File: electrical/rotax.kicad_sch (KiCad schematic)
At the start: 22 parts

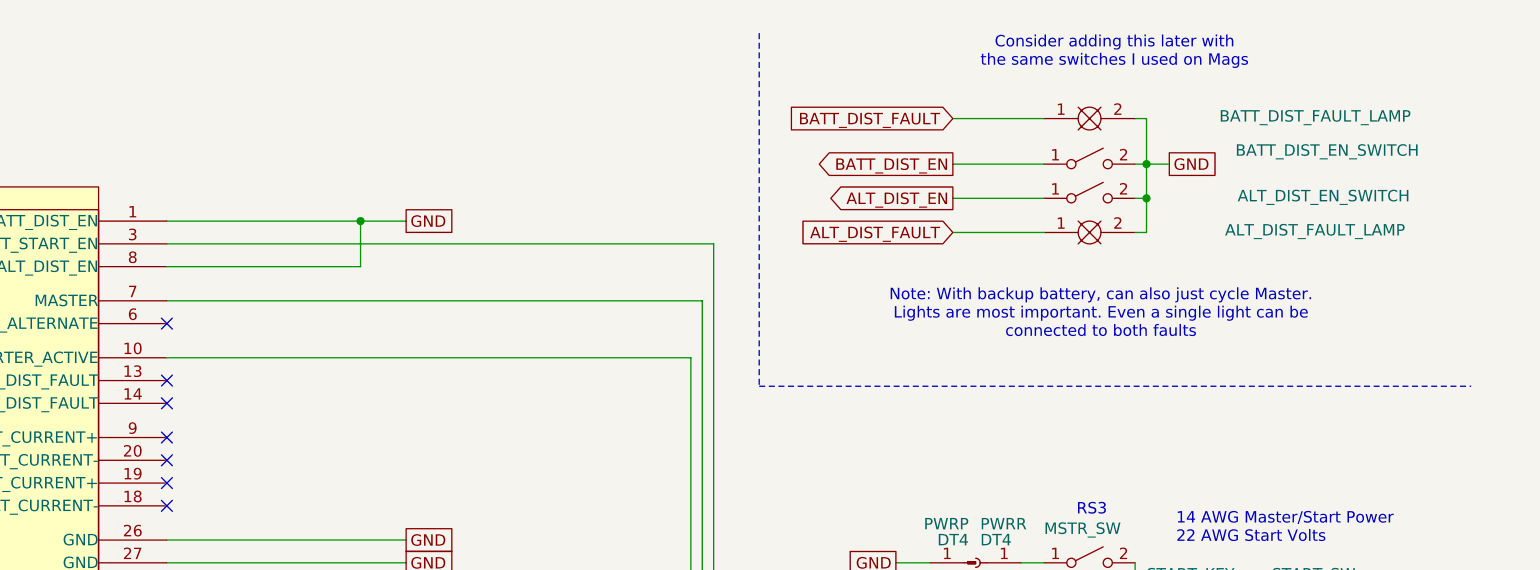
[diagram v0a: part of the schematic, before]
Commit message: Added PPS Indicator circuit
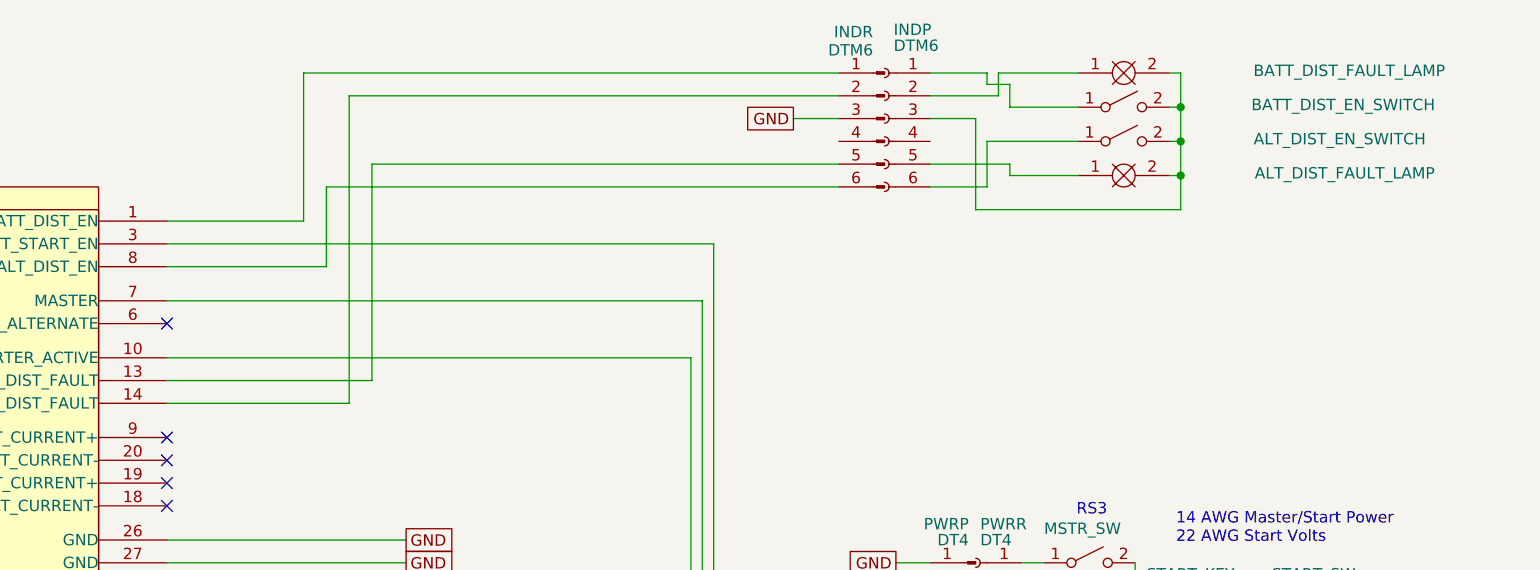
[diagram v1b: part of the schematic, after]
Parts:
- added INDP: DTM6, symbol Connector:Conn_01x06_Socket
- added INDR: DTM6, symbol Connector:Conn_01x06_Pin
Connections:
- net Earth: now also INDR.3 (Pin_3); no longer ALT_DIST_EN_SWITCH.2 (B), ALT_DIST_FAULT_LAMP.2, BATT_DIST_EN_SWITCH.2 (B), BATT_DIST_FAULT_LAMP.2, PPS.1 (BATT_DIST_EN), PPS.8 (ALT_DIST_EN)
- net at PPS.13 (ALT_DIST_FAULT): now also INDR.5 (Pin_5)
- net at PPS.14 (BATT_DIST_FAULT): now also INDR.2 (Pin_2)
- net ALT_DIST_EN: no longer names the net of ALT_DIST_EN_SWITCH.1 (A)
- net ALT_DIST_EN: now also INDP.6 (Pin_6)
- net ALT_DIST_FAULT: no longer names the net of ALT_DIST_FAULT_LAMP.1
- net ALT_DIST_FAULT: now also INDP.5 (Pin_5)
- net BATT_DIST_EN: no longer names the net of BATT_DIST_EN_SWITCH.1 (A)
- net BATT_DIST_EN: now also INDP.1 (Pin_1)
- net BATT_DIST_FAULT: no longer names the net of BATT_DIST_FAULT_LAMP.1
- net BATT_DIST_FAULT: now also INDP.2 (Pin_2)
- new net: ALT_DIST_EN_SWITCH.2 (B), ALT_DIST_FAULT_LAMP.2, BATT_DIST_EN_SWITCH.2 (B), BATT_DIST_FAULT_LAMP.2, INDP.3 (Pin_3)
- new net: INDR.1 (Pin_1), PPS.1 (BATT_DIST_EN)
- new net: INDR.6 (Pin_6), PPS.8 (ALT_DIST_EN)
- no-connect marks 10 -> 8
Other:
- note removed: "Consider adding this later with the same switches I used on Mags"
- note removed: "Note: With backup battery, can also just cycle Master. Lights are most important. Even a single light can be connected to both faults"
- moved on the sheet: ALT_DIST_EN_SWITCH, ALT_DIST_FAULT_LAMP, BATT_DIST_EN_SWITCH, BATT_DIST_FAULT_LAMP

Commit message: Corrected all rececptacle/plug polarity and naming.
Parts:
- IND: renamed from INDR; value DTM6 -> DTM6R
- IND: renamed from INDP; value DTM6 -> DTM6P
- MSTR: renamed from PWRR; value DT4 -> DT4P
- MSTR: renamed from PWRP; value DT4 -> DT4R
- PLD: renamed from IGNP; value DT6 -> DT6R
- PLD: renamed from IGNP; value DT6 -> DT6P
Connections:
- net Earth: now also MSTR.1 (Pin_1), PLD.2 (Pin_2), PLD.4 (Pin_4); no longer MSTR.1 (Pin_1), PLD.2 (Pin_2), PLD.4 (Pin_4)
- net IGN_PWR: now also PLD.3 (Pin_3); no longer PLD.3 (Pin_3)
- net START_VOLTS: now also MSTR.4 (Pin_4); no longer MSTR.4 (Pin_4)
- net at MSTR_SW.1 (A): now also MSTR.1 (Pin_1); no longer MSTR.1 (Pin_1)
- net at MSTR.2 (Pin_2): now also PPS.7 (MASTER); no longer MSTR_SW.2 (B)
- net at MSTR.3 (Pin_3): now also PPS.3 (MAIN_BATT_START_EN); no longer START_KEY.1 (A)
- net at PLD.1 (Pin_1): now also PLEADL_SW.2 (B); no longer SFLY_LEFT. (PLEAD)
- net at SFLY_RIGHT. (PLEAD): now also PLD.6 (Pin_6); no longer PLD.3 (Pin_3)
- net at PLD.6 (Pin_6): now also PLEADR_SW.2 (B); no longer SFLY_RIGHT. (PLEAD)
- net at PLD.1 (Pin_1): now also SFLY_LEFT. (PLEAD); no longer PLEADL_SW.2 (B)
- net at PLD.5 (Pin_5): now also PLD.4 (Pin_4), SFLY_RIGHT. (PLEAD)
- net at PPS.10 (STARTER_ACTIVE): now also MSTR.4 (Pin_4); no longer MSTR.4 (Pin_4)
- net at MSTR.3 (Pin_3): now also START_KEY.1 (A); no longer PPS.3 (MAIN_BATT_START_EN)
- net at MSTR.2 (Pin_2): now also MSTR_SW.2 (B); no longer PPS.7 (MASTER)
- new net: PLD.3 (Pin_3), SFLY_RIGHT. (PLEAD)
- now unconnected: PLD.5 (Pin_5)
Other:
- moved on the sheet: MSTR, PLD
